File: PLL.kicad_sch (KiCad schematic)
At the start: 88 parts, among them J301 Vtune, J302 RFShield_TwoPieces, J303 CPout, J304 DNP, J305 DNP, J306 DNP, J307 DNP, J308 DNP, U301 LMX2572, U302 XC6204B33

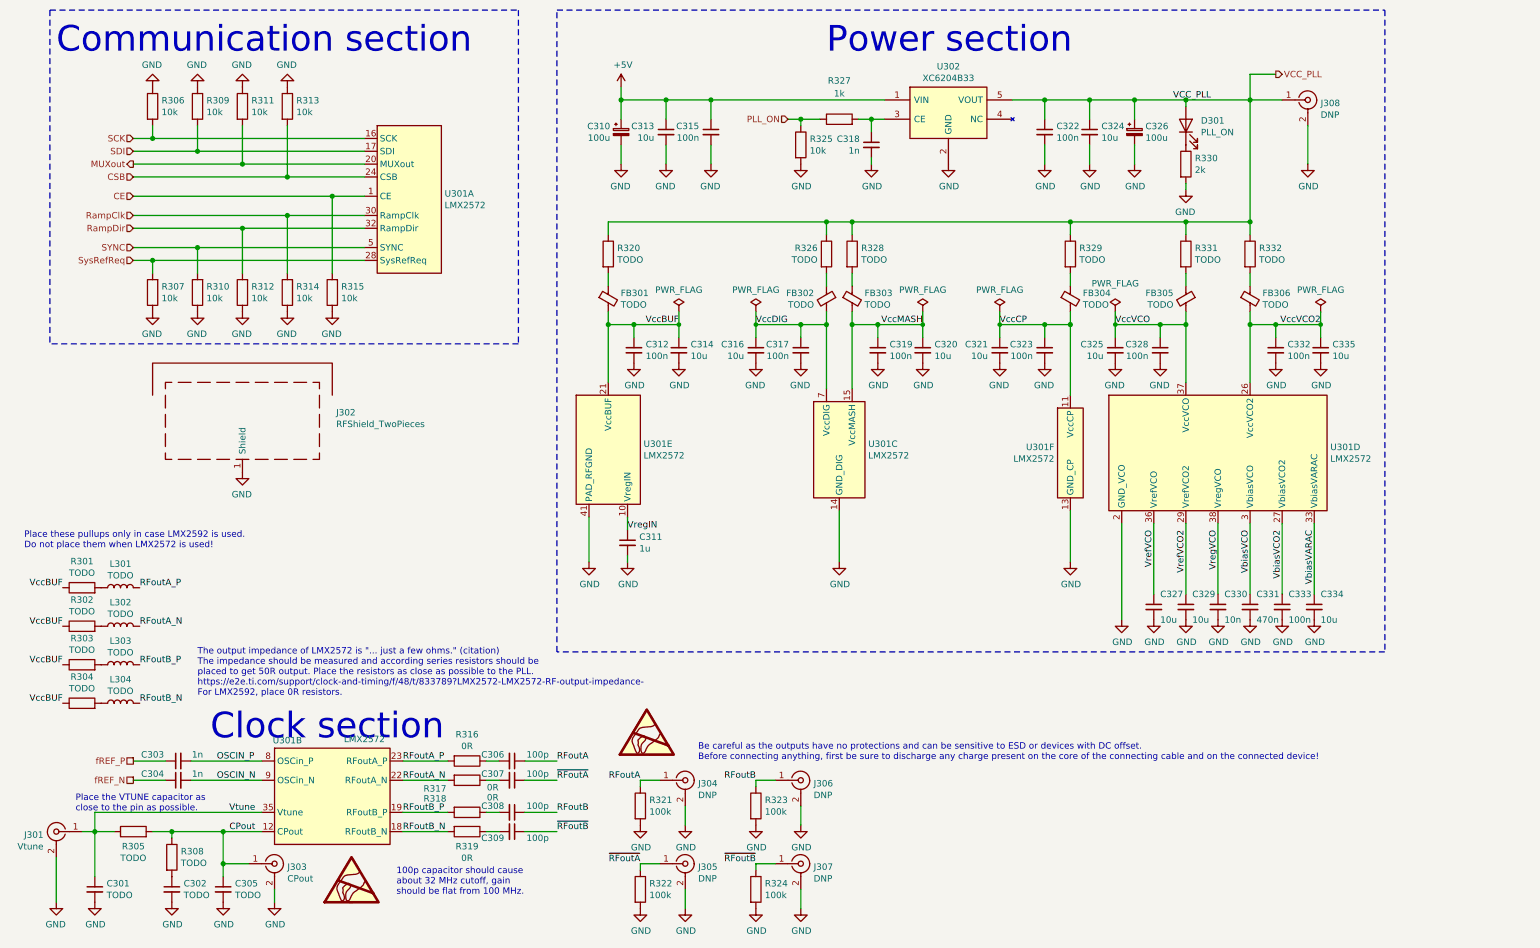
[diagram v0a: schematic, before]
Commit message: Working on making the original module a self-contained module with MCU. Added PCB.
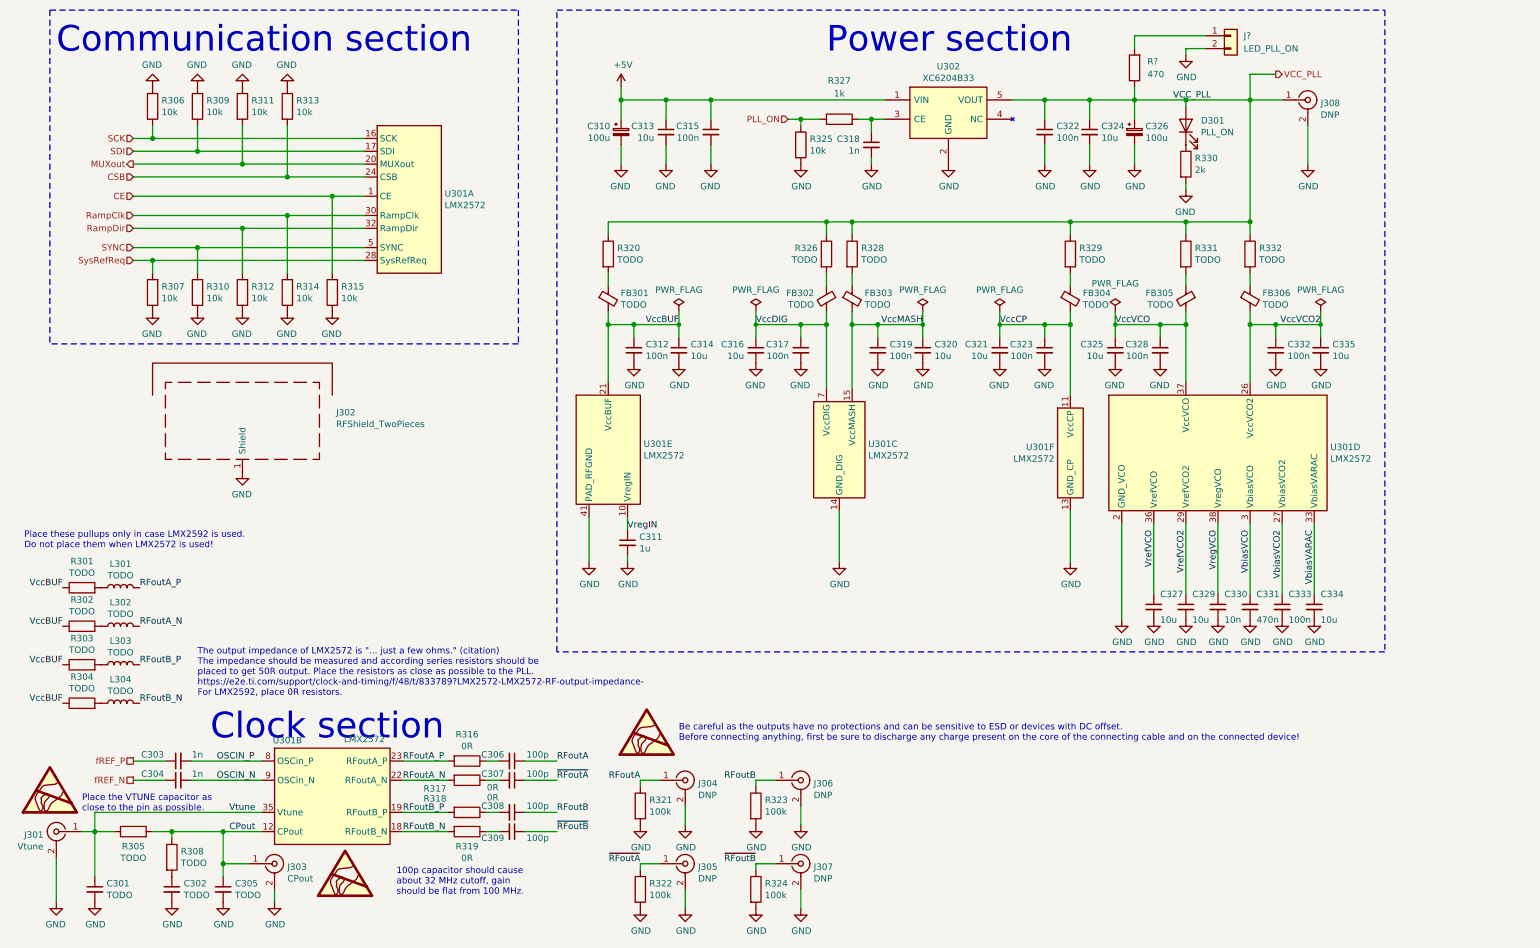
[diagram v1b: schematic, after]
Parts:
- added J?: LED_PLL_ON, symbol Connector_Generic:Conn_01x02
- added R?: 470, Resistor_SMD:R_0603_1608Metric_Pad0.98x0.95mm_HandSolder, symbol Device:R
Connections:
- net GND: now also J?.2 (Pin_2)
- net VCC_PLL: now also R?.1
- net ~RFoutA renamed ~{RFoutA}
- net ~RFoutB renamed ~{RFoutB}
- new net: J?.1 (Pin_1), R?.2

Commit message: Updates to schematic
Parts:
- removed J?: LED_PLL_ON, symbol Connector_Generic:Conn_01x02
- removed R?: 470, Resistor_SMD:R_0603_1608Metric_Pad0.98x0.95mm_HandSolder, symbol Device:R
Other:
- note added: "100p capacitor should cause about 32 MHz cutoff, gain should be flat from 100 MHz. For full range, use >270 pF."
- note removed: "100p capacitor should cause about 32 MHz cutoff, gain should be flat from 100 MHz."
- moved on the sheet: J302

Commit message: Updated schematics
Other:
- moved on the sheet: C301, C302, C303, C304, C305, C306, C307, C308, C309, J301, J302, J303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

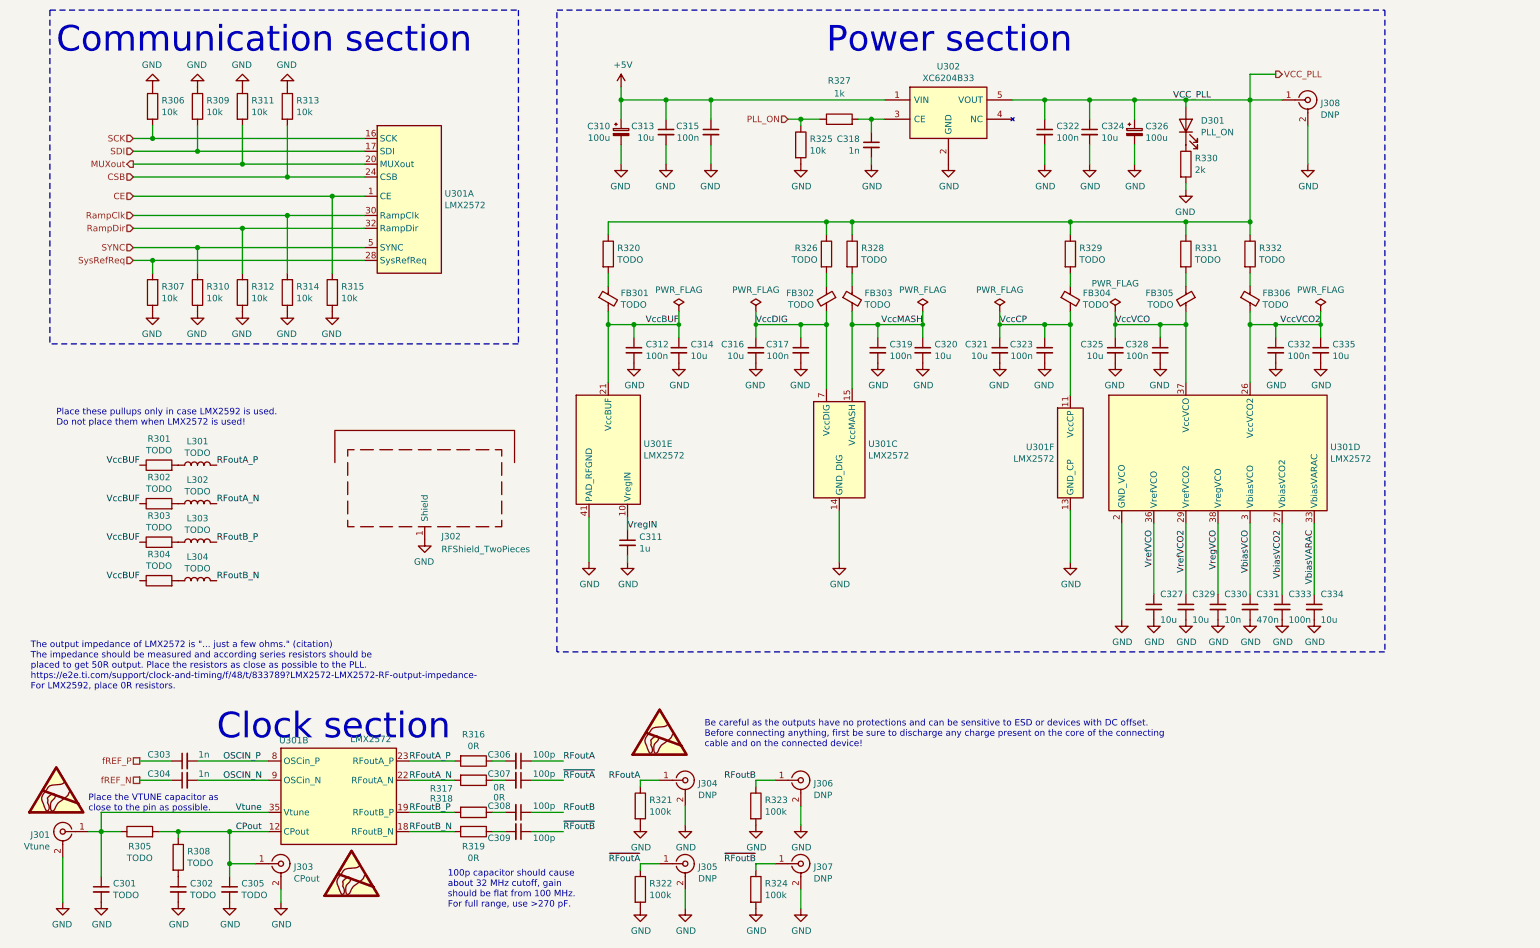
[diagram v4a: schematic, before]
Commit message: Schematic fixes
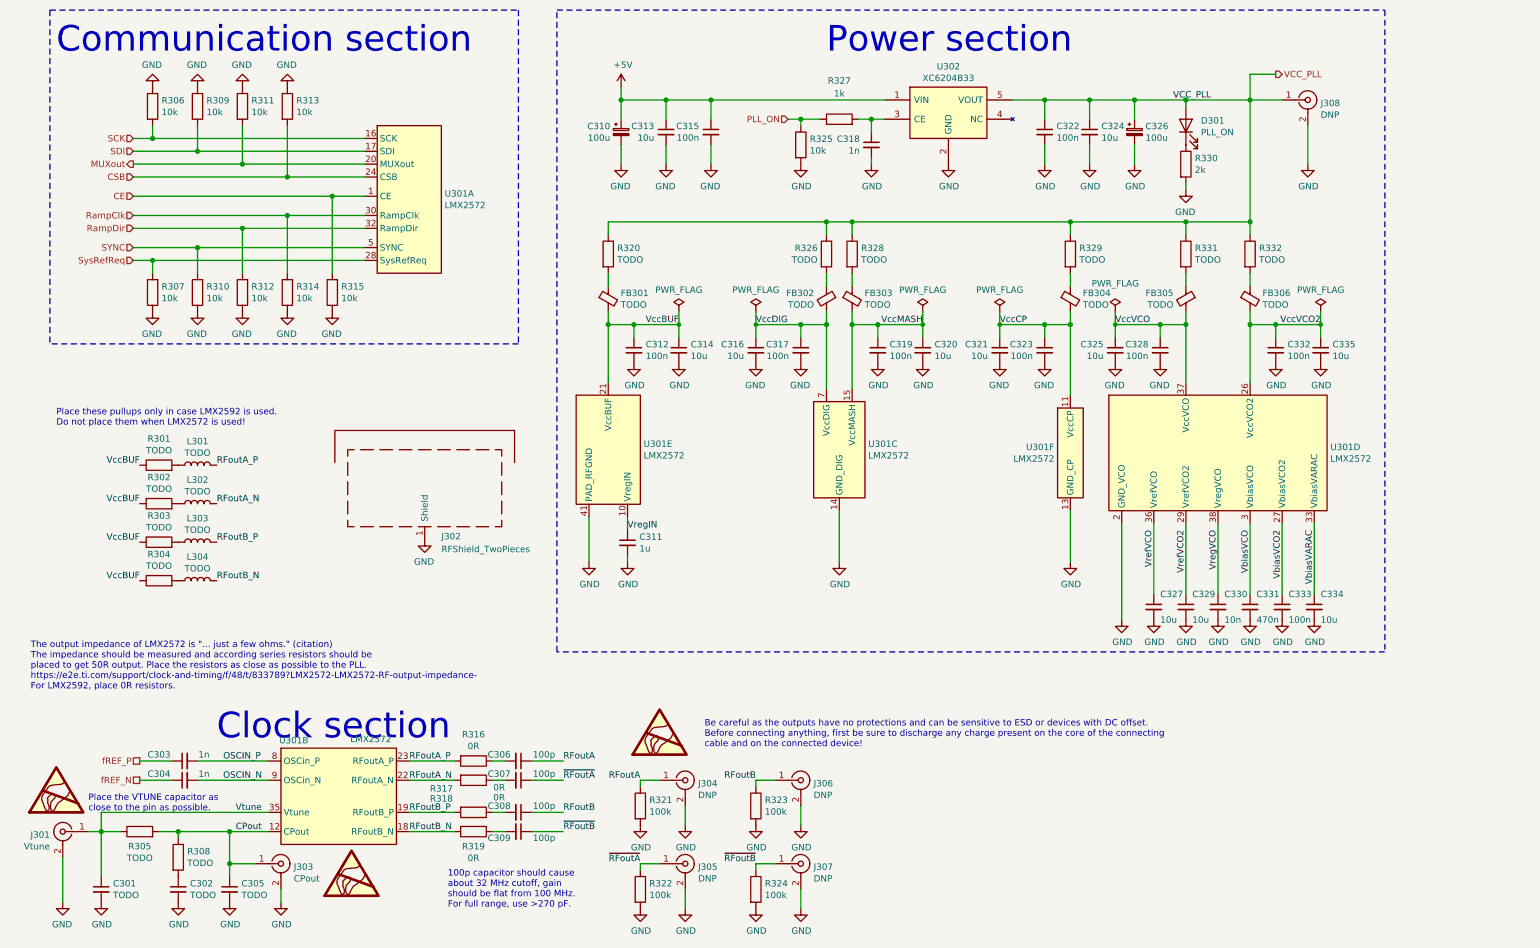
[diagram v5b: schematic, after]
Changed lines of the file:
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@@
     (comment 3 "Dual channel symmetric outputs")
   )
+  (junction (at 48.26 60.96) (diameter 1.016) (color 0 0 0 0))
+  (junction (at 177.8 76.2) (diameter 1.016) (color 0 0 0 0))
+  (junction (at 182.88 76.2) (diameter 1.016) (color 0 0 0 0))
+  (junction (at 57.15 57.15) (diameter 1.016) (color 0 0 0 0))
+  (junction (at 44.45 176.53) (diameter 1.016) (color 0 0 0 0))
+  (junction (at 181.61 35.56) (diameter 1.016) (color 0 0 0 0))
+  (junction (at 167.64 76.2) (diameter 1.016) (color 0 0 0 0))
+  (junction (at 167.64 35.56) (diameter 1.016) (color 0 0 0 0))
   (junction (at 220.98 76.2) (diameter 1.016) (color 0 0 0 0))
   (junction (at 74.93 50.8) (diameter 1.016) (color 0 0 0 0))
+  (junction (at 191.77 76.2) (diameter 0.9144) (color 0 0 0 0))
+  (junction (at 220.98 55.88) (diameter 1.016) (color 0 0 0 0))
+  (junction (at 134.62 76.2) (diameter 1.016) (color 0 0 0 0))
+  (junction (at 54.61 182.88) (diameter 1.016) (color 0 0 0 0))
+  (junction (at 54.61 176.53) (diameter 1.016) (color 0 0 0 0))
+  (junction (at 233.68 31.75) (diameter 1.016) (color 0 0 0 0))
+  (junction (at 243.84 76.2) (diameter 1.016) (color 0 0 0 0))
+  (junction (at 256.54 55.88) (diameter 1.016) (color 0 0 0 0))
+  (junction (at 39.37 63.5) (diameter 1.016) (color 0 0 0 0))
+  (junction (at 207.01 76.2) (diameter 0.9144) (color 0 0 0 0))
+  (junction (at 270.51 76.2) (diameter 0.9144) (color 0 0 0 0))
   (junction (at 66.04 46.99) (diameter 1.016) (color 0 0 0 0))
-  (junction (at 191.77 76.2) (diameter 0.9144) (color 0 0 0 0))
-  (junction (at 54.61 182.88) (diameter 1.016) (color 0 0 0 0))
+  (junction (at 243.84 31.75) (diameter 1.016) (color 0 0 0 0))
+  (junction (at 238.76 76.2) (diameter 1.016) (color 0 0 0 0))
+  (junction (at 243.84 55.88) (diameter 1.016) (color 0 0 0 0))
+  (junction (at 215.9 31.75) (diameter 1.016) (color 0 0 0 0))
+  (junction (at 66.04 54.61) (diameter 1.016) (color 0 0 0 0))
+  (junction (at 177.8 55.88) (diameter 1.016) (color 0 0 0 0))
+  (junction (at 29.21 176.53) (diameter 1.016) (color 0 0 0 0))
+  (junction (at 143.51 76.2) (diameter 0.9144) (color 0 0 0 0))
+  (junction (at 48.26 41.91) (diameter 1.016) (color 0 0 0 0))
+  (junction (at 149.86 31.75) (diameter 1.016) (color 0 0 0 0))
+  (junction (at 229.87 76.2) (diameter 0.9144) (color 0 0 0 0))
+  (junction (at 132.08 31.75) (diameter 1.016) (color 0 0 0 0))
+  (junction (at 140.97 31.75) (diameter 1.016) (color 0 0 0 0))
+  (junction (at 172.72 76.2) (diameter 1.016) (color 0 0 0 0))
+  (junction (at 39.37 39.37) (diameter 1.016) (color 0 0 0 0))
+  (junction (at 256.54 31.75) (diameter 1.016) (color 0 0 0 0))
+  (junction (at 256.54 76.2) (diameter 1.016) (color 0 0 0 0))
+  (junction (at 129.54 76.2) (diameter 1.016) (color 0 0 0 0))
+  (junction (at 215.9 76.2) (diameter 1.016) (color 0 0 0 0))
+  (junction (at 158.75 76.2) (diameter 0.9144) (color 0 0 0 0))
+  (junction (at 57.15 44.45) (diameter 1.016) (color 0 0 0 0))
+  (junction (at 224.79 31.75) (diameter 1.016) (color 0 0 0 0))
+  (junction (at 172.72 55.88) (diameter 1.016) (color 0 0 0 0))
   (junction (at 261.62 76.2) (diameter 1.016) (color 0 0 0 0))
-  (junction (at 39.37 63.5) (diameter 1.016) (color 0 0 0 0))
-  (junction (at 256.54 55.88) (diameter 1.016) (color 0 0 0 0))
-  (junction (at 233.68 31.75) (diameter 1.016) (color 0 0 0 0))
-  (junction (at 167.64 35.56) (diameter 1.016) (color 0 0 0 0))
-  (junction (at 39.37 39.37) (diameter 1.016) (color 0 0 0 0))
-  (junction (at 57.15 44.45) (diameter 1.016) (color 0 0 0 0))
-  (junction (at 172.72 55.88) (diameter 1.016) (color 0 0 0 0))
-  (junction (at 57.15 57.15) (diameter 1.016) (color 0 0 0 0))
-  (junction (at 238.76 76.2) (diameter 1.016) (color 0 0 0 0))
-  (junction (at 177.8 55.88) (diameter 1.016) (color 0 0 0 0))
-  (junction (at 134.62 76.2) (diameter 1.016) (color 0 0 0 0))
-  (junction (at 215.9 31.75) (diameter 1.016) (color 0 0 0 0))
-  (junction (at 256.54 31.75) (diameter 1.016) (color 0 0 0 0))
-  (junction (at 44.45 176.53) (diameter 1.016) (color 0 0 0 0))
-  (junction (at 243.84 55.88) (diameter 1.016) (color 0 0 0 0))
-  (junction (at 243.84 76.2) (diameter 1.016) (color 0 0 0 0))
-  (junction (at 270.51 76.2) (diameter 0.9144) (color 0 0 0 0))
-  (junction (at 256.54 76.2) (diameter 1.016) (color 0 0 0 0))
-  (junction (at 66.04 54.61) (diameter 1.016) (color 0 0 0 0))
-  (junction (at 48.26 60.96) (diameter 1.016) (color 0 0 0 0))
-  (junction (at 143.51 76.2) (diameter 0.9144) (color 0 0 0 0))
-  (junction (at 172.72 76.2) (diameter 1.016) (color 0 0 0 0))
-  (junction (at 129.54 76.2) (diameter 1.016) (color 0 0 0 0))
-  (junction (at 181.61 35.56) (diameter 1.016) (color 0 0 0 0))
-  (junction (at 149.86 31.75) (diameter 1.016) (color 0 0 0 0))
-  (junction (at 243.84 31.75) (diameter 1.016) (color 0 0 0 0))
-  (junction (at 132.08 31.75) (diameter 1.016) (color 0 0 0 0))
-  (junction (at 167.64 76.2) (diameter 1.016) (color 0 0 0 0))
-  (junction (at 140.97 31.75) (diameter 1.016) (color 0 0 0 0))
-  (junction (at 177.8 76.2) (diameter 1.016) (color 0 0 0 0))
-  (junction (at 54.61 176.53) (diameter 1.016) (color 0 0 0 0))
-  (junction (at 215.9 76.2) (diameter 1.016) (color 0 0 0 0))
-  (junction (at 48.26 41.91) (diameter 1.016) (color 0 0 0 0))
-  (junction (at 224.79 31.75) (diameter 1.016) (color 0 0 0 0))
-  (junction (at 29.21 176.53) (diameter 1.016) (color 0 0 0 0))
-  (junction (at 207.01 76.2) (diameter 0.9144) (color 0 0 0 0))
-  (junction (at 229.87 76.2) (diameter 0.9144) (color 0 0 0 0))
-  (junction (at 158.75 76.2) (diameter 0.9144) (color 0 0 0 0))
-  (junction (at 220.98 55.88) (diameter 1.016) (color 0 0 0 0))
-  (junction (at 182.88 76.2) (diameter 1.016) (color 0 0 0 0))
   (wire (pts (xy 220.98 68.58) (xy 220.98 66.04))
     (stroke (width 0) (type solid) (color 0 0 0 0))
@@
     (stroke (width 0) (type solid) (color 0 0 0 0))
   )
+  (wire (pts (xy 233.68 31.75) (xy 243.84 31.75))
+    (stroke (width 0) (type solid) (color 0 0 0 0))
+  )
   (wire (pts (xy 243.84 31.75) (xy 256.54 31.75))
     (stroke (width 0) (type solid) (color 0 0 0 0))
@@
     (stroke (width 0) (type solid) (color 0 0 0 0))
   )
-  (wire (pts (xy 233.68 31.75) (xy 243.84 31.75))
-    (stroke (width 0) (type solid) (color 0 0 0 0))
-  )
   (wire (pts (xy 256.54 31.75) (xy 256.54 55.88))
     (stroke (width 0) (type solid) (color 0 0 0 0))
@@
     (stroke (width 0) (type solid) (color 0 0 0 0))
   )
+  (polyline (pts (xy 19.05 13.97) (xy 19.05 80.01))
+    (stroke (width 0) (type dash) (color 0 0 0 0))
+  )
+  (polyline (pts (xy 19.05 13.97) (xy 111.76 13.97))
+    (stroke (width 0) (type dash) (color 0 0 0 0))
+  )
+  (polyline (pts (xy 111.76 80.01) (xy 19.05 80.01))
+    (stroke (width 0) (type dash) (color 0 0 0 0))
+  )
   (polyline (pts (xy 111.76 13.97) (xy 111.76 80.01))
     (stroke (width 0) (type dash) (color 0 0 0 0))
   )
-  (polyline (pts (xy 19.05 13.97) (xy 111.76 13.97))
-    (stroke (width 0) (type dash) (color 0 0 0 0))
-  )
-  (polyline (pts (xy 19.05 13.97) (xy 19.05 80.01))
-    (stroke (width 0) (type dash) (color 0 0 0 0))
-  )
-  (polyline (pts (xy 111.76 80.01) (xy 19.05 80.01))
-    (stroke (width 0) (type dash) (color 0 0 0 0))
-  )
   (wire (pts (xy 177.8 76.2) (xy 177.8 73.66))
     (stroke (width 0) (type solid) (color 0 0 0 0))
@@
     (stroke (width 0) (type solid) (color 0 0 0 0))
   )
+  (polyline (pts (xy 283.21 13.97) (xy 283.21 140.97))
+    (stroke (width 0) (type dash) (color 0 0 0 0))
+  )
+  (polyline (pts (xy 283.21 140.97) (xy 119.38 140.97))
+    (stroke (width 0) (type dash) (color 0 0 0 0))
+  )
+  (polyline (pts (xy 119.38 140.97) (xy 119.38 13.97))
+    (stroke (width 0) (type dash) (color 0 0 0 0))
+  )
+  (polyline (pts (xy 123.19 13.97) (xy 283.21 13.97))
+    (stroke (width 0) (type dash) (color 0 0 0 0))
+  )
   (polyline (pts (xy 119.38 13.97) (xy 123.19 13.97))
     (stroke (width 0) (type dash) (color 0 0 0 0))
   )
-  (polyline (pts (xy 283.21 13.97) (xy 283.21 140.97))
-    (stroke (width 0) (type dash) (color 0 0 0 0))
-  )
-  (polyline (pts (xy 123.19 13.97) (xy 283.21 13.97))
-    (stroke (width 0) (type dash) (color 0 0 0 0))
-  )
-  (polyline (pts (xy 283.21 140.97) (xy 119.38 140.97))
-    (stroke (width 0) (type dash) (color 0 0 0 0))
-  )
-  (polyline (pts (xy 119.38 140.97) (xy 119.38 13.97))
-    (stroke (width 0) (type dash) (color 0 0 0 0))
-  )
